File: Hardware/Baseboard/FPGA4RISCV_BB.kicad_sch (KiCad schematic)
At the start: 0 parts

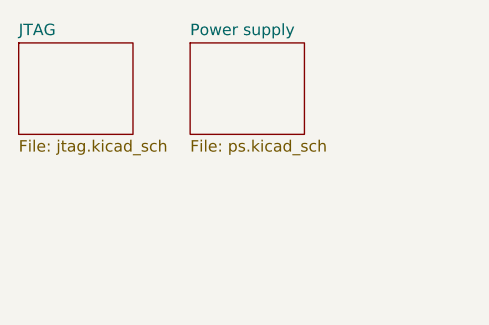
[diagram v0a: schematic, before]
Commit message: SOM board outline
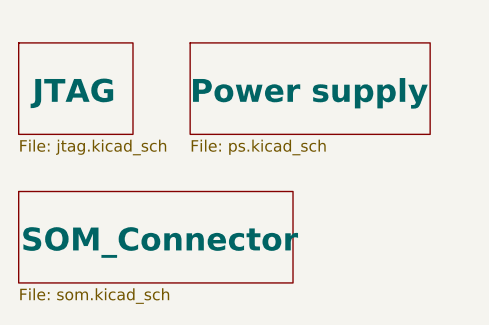
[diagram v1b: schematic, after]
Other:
- added sheet SOM_Connector (som.kicad_sch)
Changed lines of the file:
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@@
 	(paper "A4")
 	(sheet
-		(at 76.2 52.07)
-		(size 12.7 10.16)
+		(at 57.15 68.58)
+		(size 30.48 10.16)
 		(exclude_from_sim no)
 		(in_bom yes)
 		(on_board yes)
 		(dnp no)
-		(fields_autoplaced yes)
+		(stroke
+			(width 0.1524)
+			(type solid)
+		)
+		(fill
+			(color 0 0 0 0.0000)
+		)
+		(property "Sheetname" "SOM_Connector"
+			(at 57.404 75.438 0)
+			(effects
+				(font
+					(size 2.54 2.54)
+					(thickness 0.508)
+					(bold yes)
+				)
+				(justify left bottom)
+			)
+		)
+		(property "Sheetfile" "som.kicad_sch"
+			(at 57.15 79.3246 0)
+			(effects
+				(font
+					(size 1.27 1.27)
+				)
+				(justify left top)
+			)
+		)
+		(instances
+			(project "FPGA4RISCV_BB"
+				(path "/de32abb0-ff3b-4c67-a91a-eed08140b1b2"
+					(page "3")
+				)
+			)
+		)
+	)
+	(sheet
+		(at 76.2 52.07)
+		(size 26.67 10.16)
+		(exclude_from_sim no)
+		(in_bom yes)
+		(on_board yes)
+		(dnp no)
 		(stroke
 			(width 0.1524)
@@
 		)
 		(property "Sheetname" "Power supply"
-			(at 76.2 51.3584 0)
+			(at 76.2 58.928 0)
 			(effects
 				(font
-					(size 1.27 1.27)
+					(size 2.54 2.54)
+					(thickness 0.508)
+					(bold yes)
 				)
 				(justify left bottom)
@@
 		(on_board yes)
 		(dnp no)
-		(fields_autoplaced yes)
 		(stroke
 			(width 0.1524)
@@
 		)
 		(property "Sheetname" "JTAG"
-			(at 57.15 51.3584 0)
+			(at 58.674 58.928 0)
 			(effects
 				(font
-					(size 1.27 1.27)
+					(size 2.54 2.54)
+					(thickness 0.508)
+					(bold yes)
 				)
 				(justify left bottom)

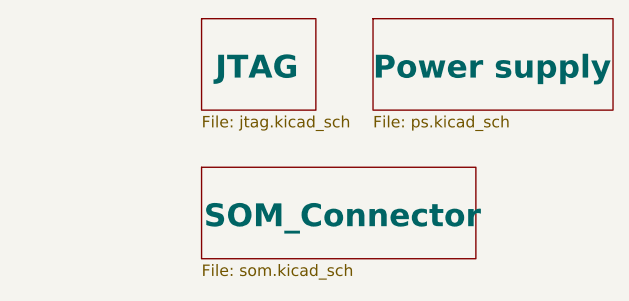
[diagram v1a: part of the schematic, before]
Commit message: QSPI, banks IO decoupling
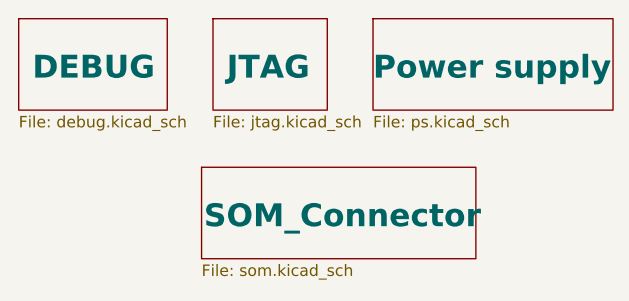
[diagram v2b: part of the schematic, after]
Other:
- added sheet DEBUG (debug.kicad_sch)
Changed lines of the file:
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@@
 	)
 	(sheet
-		(at 57.15 52.07)
+		(at 36.83 52.07)
+		(size 16.51 10.16)
+		(exclude_from_sim no)
+		(in_bom yes)
+		(on_board yes)
+		(dnp no)
+		(stroke
+			(width 0.1524)
+			(type solid)
+		)
+		(fill
+			(color 0 0 0 0.0000)
+		)
+		(property "Sheetname" "DEBUG"
+			(at 38.354 58.928 0)
+			(effects
+				(font
+					(size 2.54 2.54)
+					(thickness 0.508)
+					(bold yes)
+				)
+				(justify left bottom)
+			)
+		)
+		(property "Sheetfile" "debug.kicad_sch"
+			(at 36.83 62.8146 0)
+			(effects
+				(font
+					(size 1.27 1.27)
+				)
+				(justify left top)
+			)
+		)
+		(instances
+			(project "FPGA4RISCV_BB"
+				(path "/de32abb0-ff3b-4c67-a91a-eed08140b1b2"
+					(page "4")
+				)
+			)
+		)
+	)
+	(sheet
+		(at 58.42 52.07)
 		(size 12.7 10.16)
 		(exclude_from_sim no)
@@
 		)
 		(property "Sheetname" "JTAG"
-			(at 58.674 58.928 0)
+			(at 59.944 58.928 0)
 			(effects
 				(font
@@
 		)
 		(property "Sheetfile" "jtag.kicad_sch"
-			(at 57.15 62.8146 0)
+			(at 58.42 62.8146 0)
 			(effects
 				(font

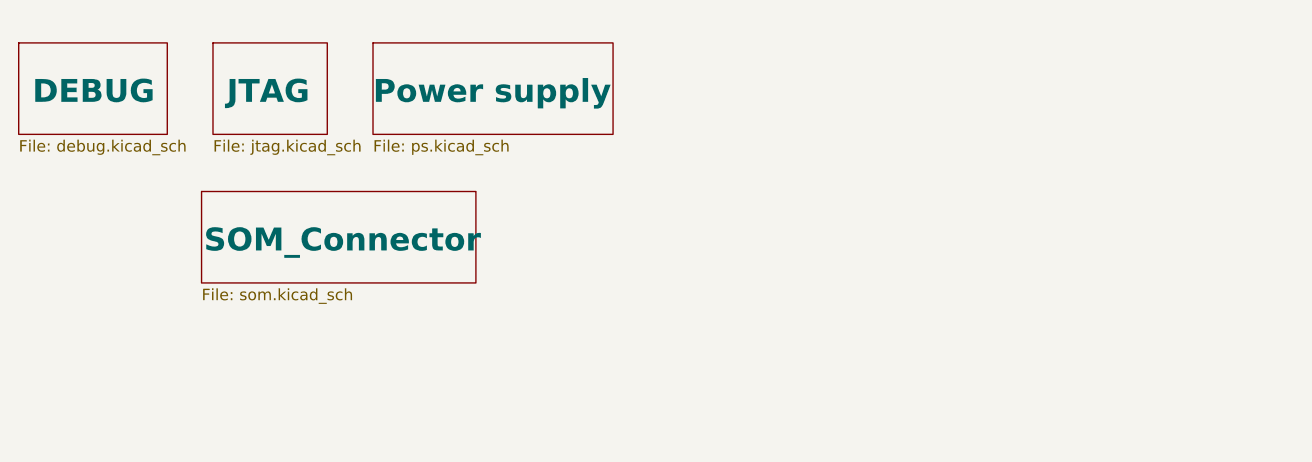
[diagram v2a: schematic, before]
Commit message: M.2 connector added
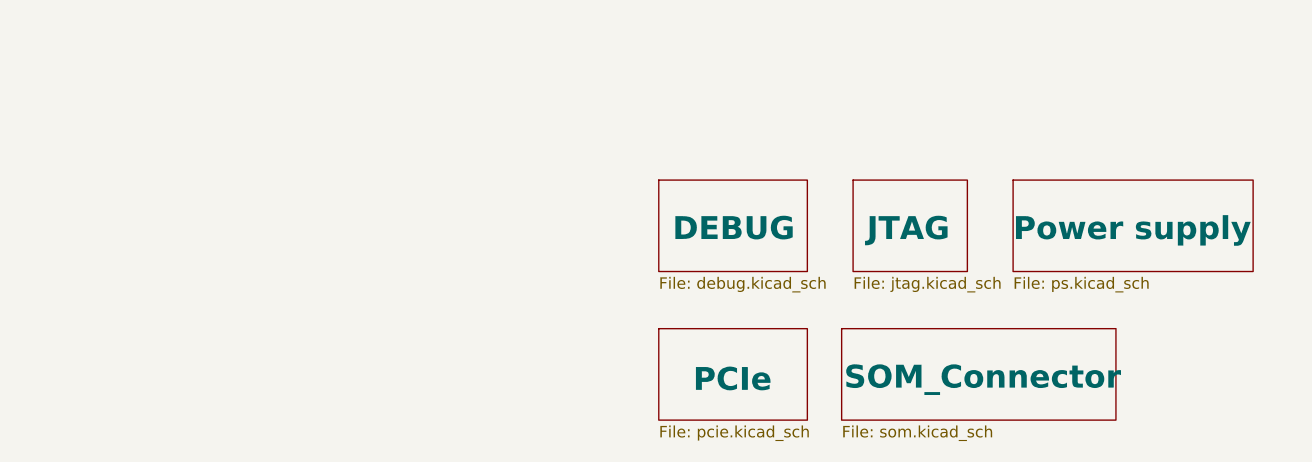
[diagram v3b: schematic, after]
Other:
- added sheet PCIe (pcie.kicad_sch)
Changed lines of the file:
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@@
 	(paper "A4")
 	(sheet
-		(at 57.15 68.58)
+		(at 128.27 83.82)
 		(size 30.48 10.16)
 		(exclude_from_sim no)
@@
 		)
 		(property "Sheetname" "SOM_Connector"
-			(at 57.404 75.438 0)
+			(at 128.524 90.678 0)
 			(effects
 				(font
@@
 		)
 		(property "Sheetfile" "som.kicad_sch"
-			(at 57.15 79.3246 0)
+			(at 128.27 94.5646 0)
 			(effects
 				(font
@@
 	)
 	(sheet
-		(at 76.2 52.07)
+		(at 147.32 67.31)
 		(size 26.67 10.16)
 		(exclude_from_sim no)
@@
 		)
 		(property "Sheetname" "Power supply"
-			(at 76.2 58.928 0)
+			(at 147.32 74.168 0)
 			(effects
 				(font
@@
 		)
 		(property "Sheetfile" "ps.kicad_sch"
-			(at 76.2 62.8146 0)
+			(at 147.32 78.0546 0)
 			(effects
 				(font
@@
 	)
 	(sheet
-		(at 36.83 52.07)
+		(at 107.95 67.31)
 		(size 16.51 10.16)
 		(exclude_from_sim no)
@@
 		)
 		(property "Sheetname" "DEBUG"
-			(at 38.354 58.928 0)
+			(at 109.474 74.168 0)
 			(effects
 				(font
@@
 		)
 		(property "Sheetfile" "debug.kicad_sch"
-			(at 36.83 62.8146 0)
+			(at 107.95 78.0546 0)
 			(effects
 				(font
@@
 	)
 	(sheet
-		(at 58.42 52.07)
+		(at 107.95 83.82)
+		(size 16.51 10.16)
+		(exclude_from_sim no)
+		(in_bom yes)
+		(on_board yes)
+		(dnp no)
+		(stroke
+			(width 0.1524)
+			(type solid)
+		)
+		(fill
+			(color 0 0 0 0.0000)
+		)
+		(property "Sheetname" "PCIe"
+			(at 111.76 90.932 0)
+			(effects
+				(font
+					(size 2.54 2.54)
+					(thickness 0.508)
+					(bold yes)
+				)
+				(justify left bottom)
+			)
+		)
+		(property "Sheetfile" "pcie.kicad_sch"
+			(at 107.95 94.5646 0)
+			(effects
+				(font
+					(size 1.27 1.27)
+				)
+				(justify left top)
+			)
+		)
+		(instances
+			(project "FPGA4RISCV_BB"
+				(path "/de32abb0-ff3b-4c67-a91a-eed08140b1b2"
+					(page "6")
+				)
+			)
+		)
+	)
+	(sheet
+		(at 129.54 67.31)
 		(size 12.7 10.16)
 		(exclude_from_sim no)
@@
 		)
 		(property "Sheetname" "JTAG"
-			(at 59.944 58.928 0)
+			(at 131.064 74.168 0)
 			(effects
 				(font
@@
 		)
 		(property "Sheetfile" "jtag.kicad_sch"
-			(at 58.42 62.8146 0)
+			(at 129.54 78.0546 0)
 			(effects
 				(font
